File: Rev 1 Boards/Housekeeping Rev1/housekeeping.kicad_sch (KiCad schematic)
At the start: 36 parts, among them U13 MC34063A, U14 MC34063A, U15 MC34063A, U16 MC34063A

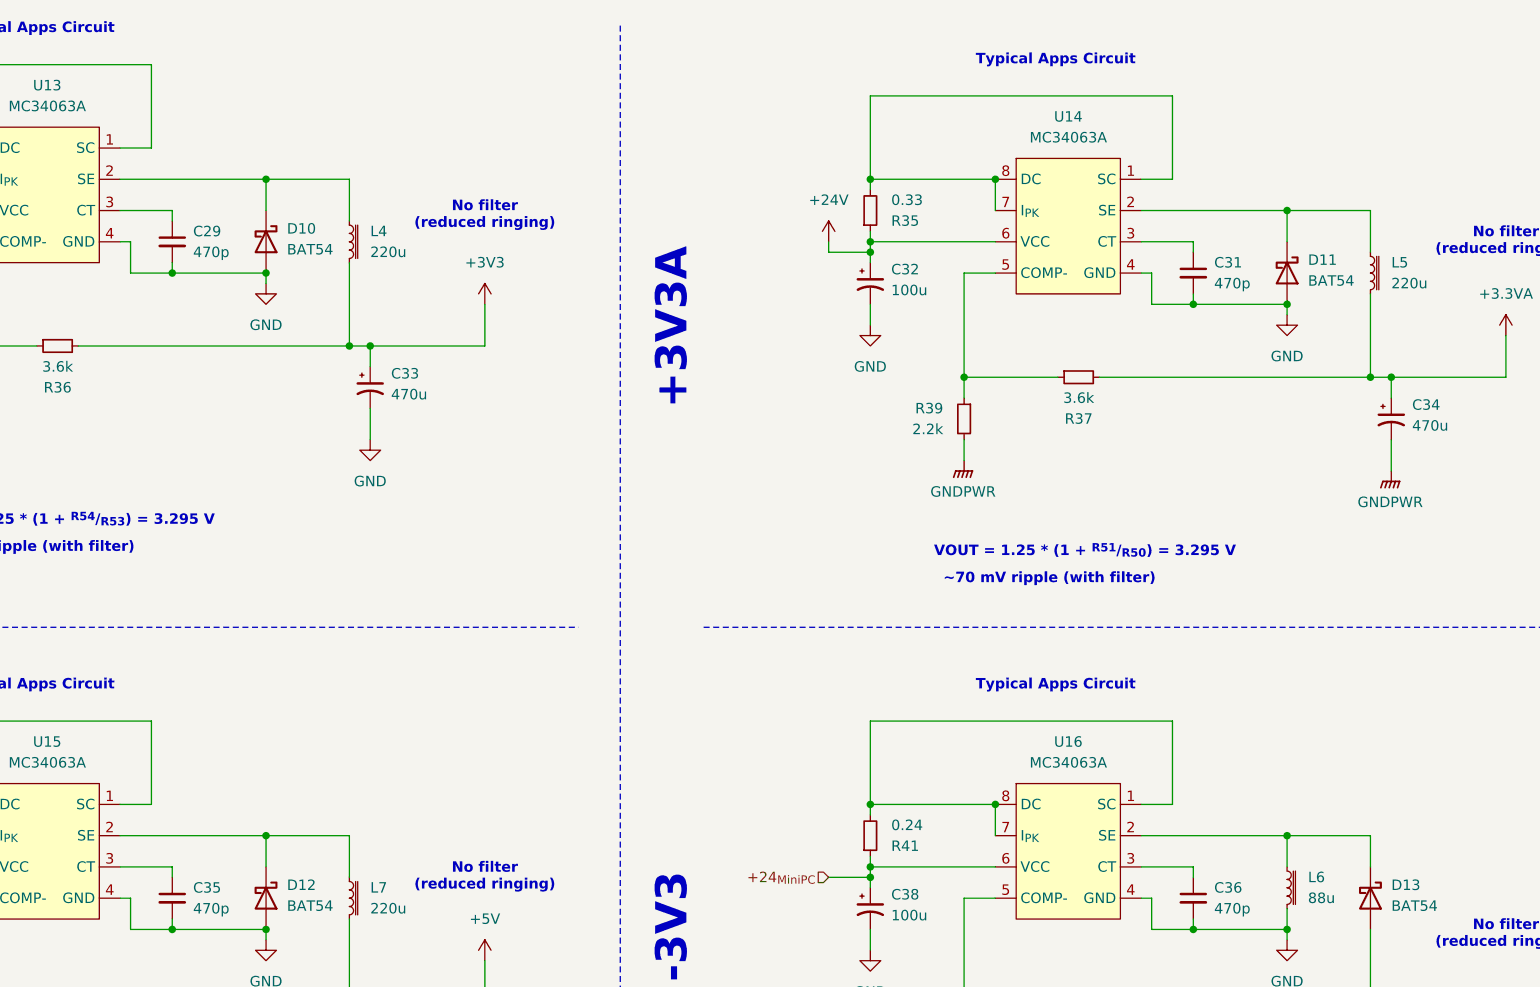
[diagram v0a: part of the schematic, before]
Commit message: beginning layout work for housekeeping pcb
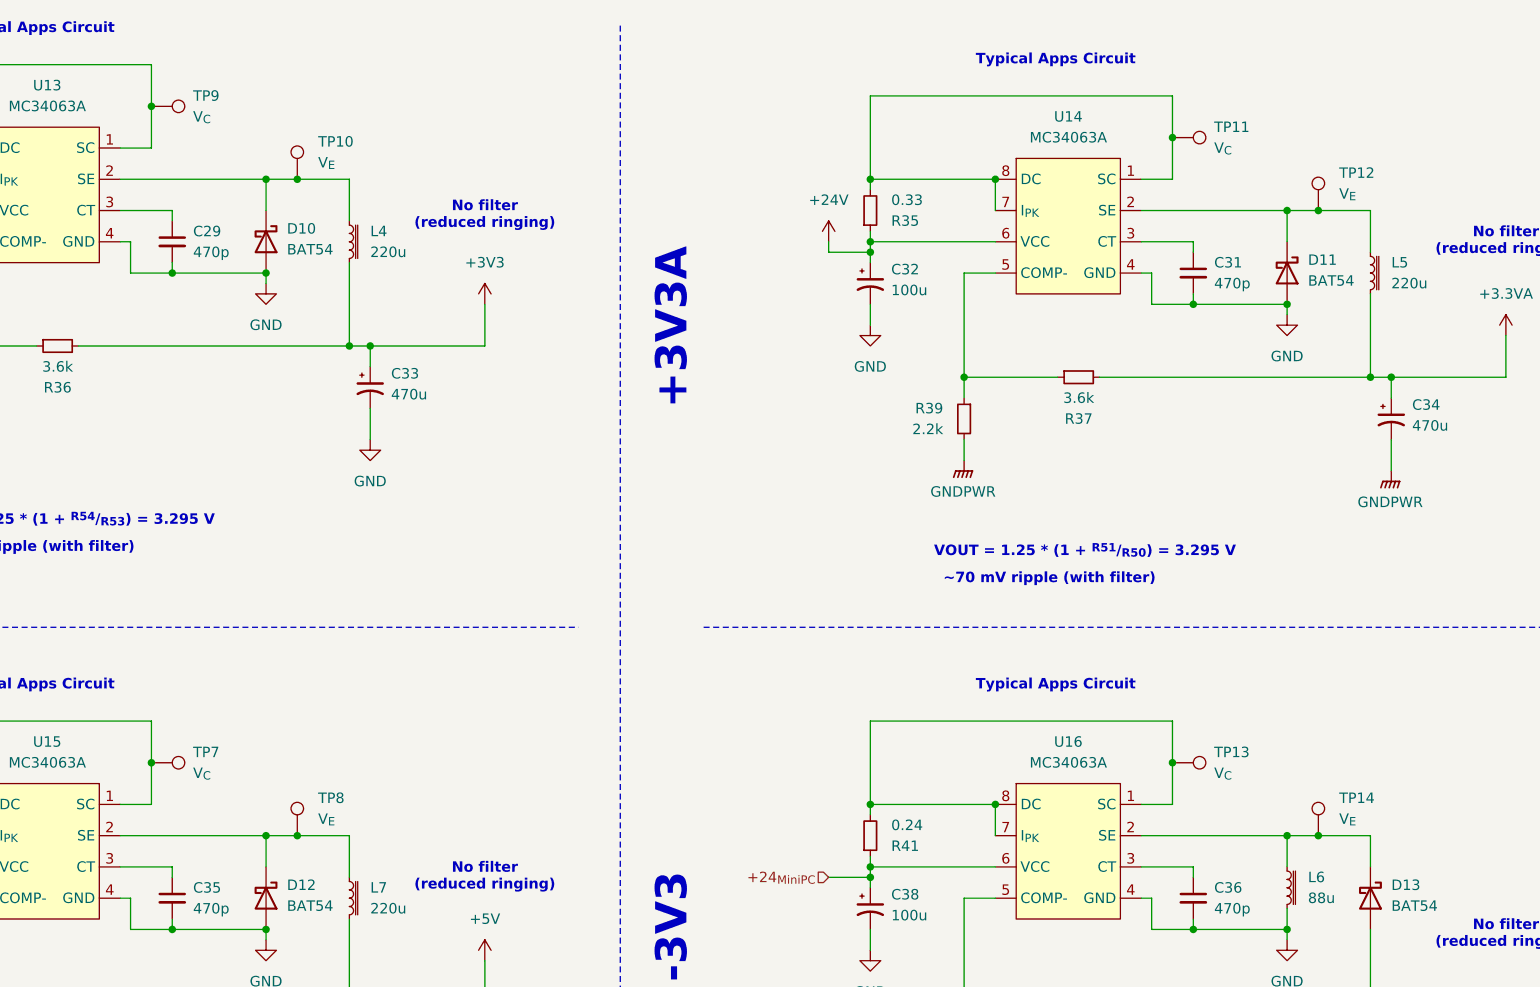
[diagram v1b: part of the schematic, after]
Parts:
- added TP10, TP12, TP14, TP8: V_{E}, TestPoint:TestPoint_Bridge_Pitch2.0mm_Drill0.7mm, symbol Connector:TestPoint
- added TP11, TP13, TP7, TP9: V_{C}, TestPoint:TestPoint_Bridge_Pitch2.0mm_Drill0.7mm, symbol Connector:TestPoint
- C29, C31, C35, C36: footprint (none) -> Capacitor_SMD:C_0603_1608Metric_Pad1.08x0.95mm_HandSolder
- L4, L5, L6, L7: footprint (none) -> ! Robomaster Passives:ASPIAIGS6055221MT; Mouser Part Number (none) -> 815-ASPIAIGS6055221T
- R34, R35, R40: footprint (none) -> Resistor_SMD:R_0603_1608Metric_Pad0.98x0.95mm_HandSolder; Mouser Part Number (none) -> 667-ERJ-3RQFR33V
- R36, R37, R42, R45: footprint (none) -> Resistor_SMD:R_0603_1608Metric_Pad0.98x0.95mm_HandSolder; Mouser Part Number (none) -> 603-RT0603FRE133K6L
- R38, R39, R43: footprint (none) -> Resistor_SMD:R_0603_1608Metric_Pad0.98x0.95mm_HandSolder; Mouser Part Number (none) -> 755-ESR03EZPJ222
- R41: footprint (none) -> Resistor_SMD:R_0603_1608Metric_Pad0.98x0.95mm_HandSolder; Mouser Part Number (none) -> 603-RL0603JR-070R24L
- R44: footprint (none) -> Resistor_SMD:R_0603_1608Metric_Pad0.98x0.95mm_HandSolder; Mouser Part Number (none) -> 603-RT0603FRE071K2L
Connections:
- net at R34.2, U13.1 (SC), U13.7 (I_{PK})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: now also TP9.1
- net at D10.3 (K), L4.1, U13.2 (SE): now also TP10.1
- net at R35.2, U14.1 (SC), U14.7 (I_{PK})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: now also TP11.1
- net at R41.2, U16.1 (SC), U16.7 (I_{PK})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: now also TP13.1
- net at D13.3 (K), L6.1, U16.2 (SE): now also TP14.1
- net at D11.3 (K), L5.1, U14.2 (SE): now also TP12.1
- net at D12.3 (K), L7.1, U15.2 (SE): now also TP8.1
- net at R40.2, U15.1 (SC), U15.7 (I_{PK})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: now also TP7.1
